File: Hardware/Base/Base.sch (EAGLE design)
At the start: 1 part

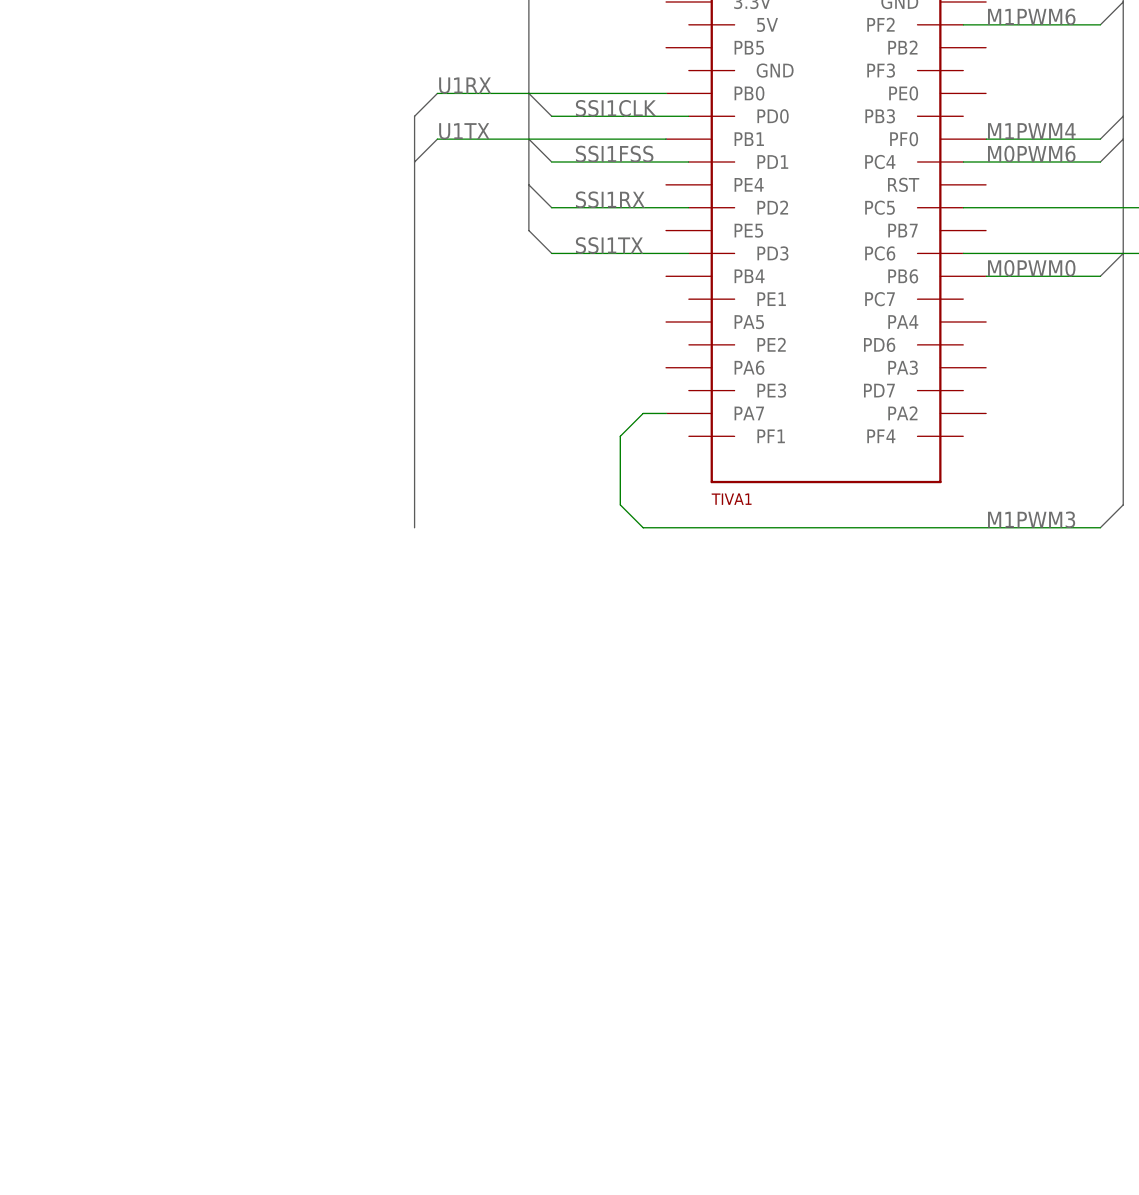
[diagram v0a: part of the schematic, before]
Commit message: Add Xbee to base schematic.
Add status LEDs to Tiva/Xbee communication.
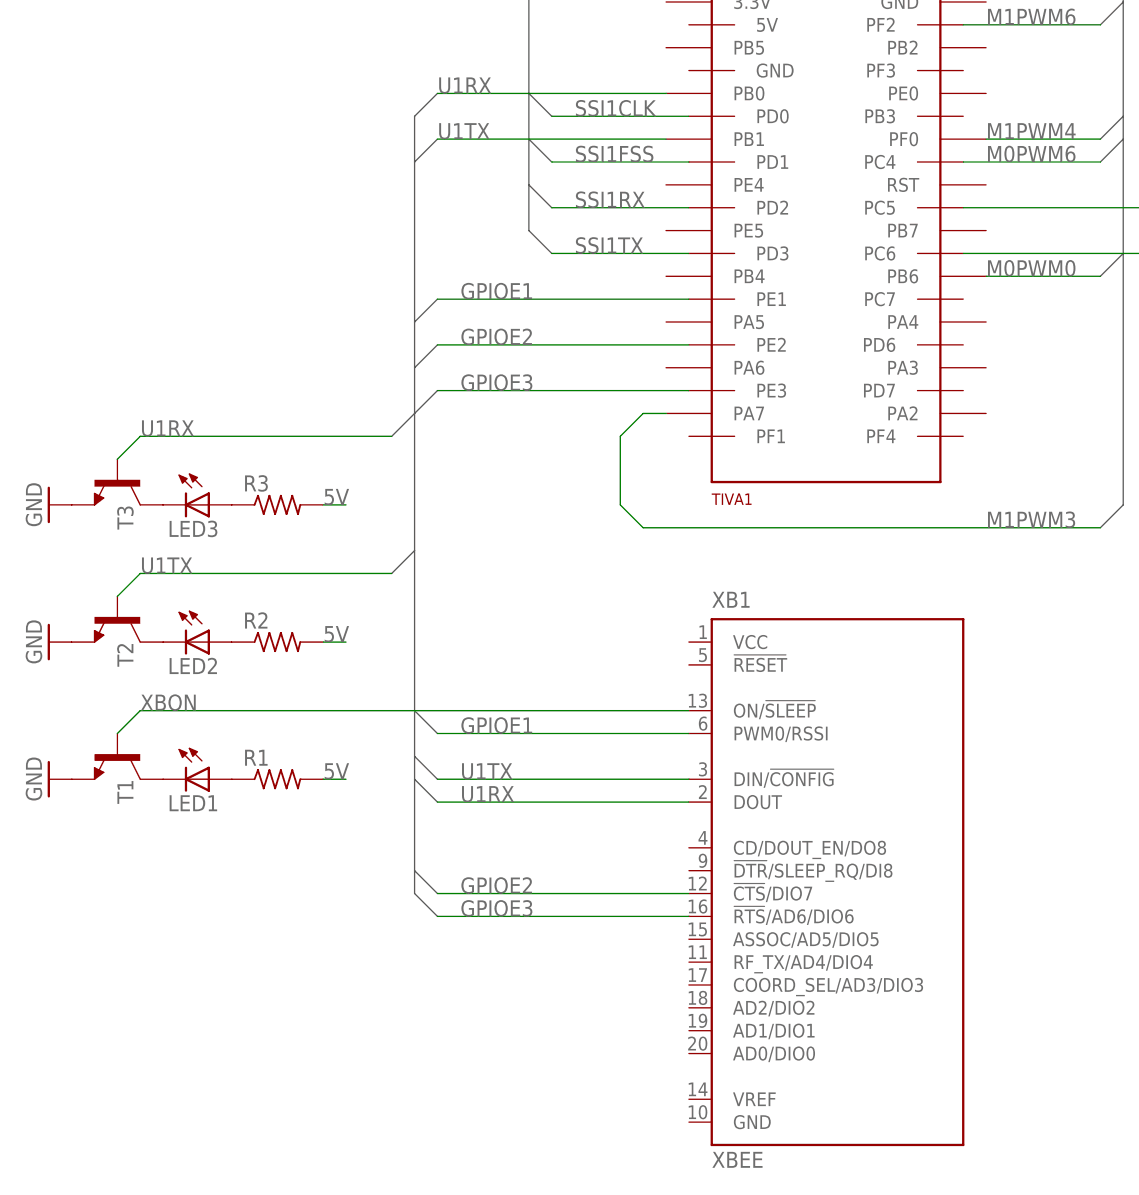
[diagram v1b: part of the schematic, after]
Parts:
- added LED1, LED2, LED3: (no value), led:LED5MM
- added R1, R2, R3: (no value), rcl:R-US_0207/7
- added T1, T2, T3: 2N3904, transistor:2N3904
- added XB1: XBEE, maxstream:XBEE
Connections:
- new net 5V: R1.2, R2.2, R3.2
- new net GND: T1.E, T2.E, T3.E
- new net GPIOE1: TIVA1.PE1, XB1.PWM0/RSSI
- new net GPIOE2: TIVA1.PE2, XB1.!CTS!/DIO7
- new net GPIOE3: TIVA1.PE3, XB1.!RTS!/AD6/DIO6
- new net N$1: LED1.C, T1.C
- new net N$2: LED2.C, T2.C
- new net N$3: LED2.A, R2.1
- new net N$4: LED1.A, R1.1
- new net N$5: LED3.C, T3.C
- new net N$6: LED3.A, R3.1
- new net XBON: T1.B, XB1.ON/!SLEEP
- net U1RX: now also T3.B, XB1.DOUT
- net U1TX: now also T2.B, XB1.DIN/!CONFIG
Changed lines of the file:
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@@
 <setting verticaltext="up"/>
 </settings>
-<grid distance="0.1" unitdist="inch" unit="mil" style="lines" multiple="1" display="yes" altdistance="0.01" altunitdist="inch" altunit="mil"/>
+<grid distance="0.1" unitdist="inch" unit="inch" style="lines" multiple="1" display="yes" altdistance="0.01" altunitdist="inch" altunit="inch"/>
 <layers>
 <layer number="1" name="Top" color="4" fill="1" visible="no" active="no"/>
@@
 <parts>
 <part name="TIVA1" library="tiva-board" deviceset="TIVA-BOARD" device=""/>
+<part name="XB1" library="maxstream" deviceset="XBEE" device=""/>
+<part name="T1" library="transistor" deviceset="2N3904" device=""/>
+<part name="R1" library="rcl" deviceset="R-US_" device="0207/7"/>
+<part name="LED1" library="led" deviceset="LED" device="5MM"/>
+<part name="GND1" library="supply1" deviceset="GND" device=""/>
+<part name="T2" library="transistor" deviceset="2N3904" device=""/>
+<part name="R2" library="rcl" deviceset="R-US_" device="0207/7"/>
+<part name="LED2" library="led" deviceset="LED" device="5MM"/>
+<part name="GND2" library="supply1" deviceset="GND" device=""/>
+<part name="T3" library="transistor" deviceset="2N3904" device=""/>
+<part name="R3" library="rcl" deviceset="R-US_" device="0207/7"/>
+<part name="LED3" library="led" deviceset="LED" device="5MM"/>
+<part name="GND3" library="supply1" deviceset="GND" device=""/>
 </parts>
 <sheets>
@@
 <instances>
 <instance part="TIVA1" gate="TIVA" x="0" y="0"/>
+<instance part="XB1" gate="G$1" x="12.7" y="-43.18"/>
+<instance part="T1" gate="G1" x="-66.04" y="-30.48" smashed="yes" rot="R270">
+<attribute name="NAME" x="-66.04" y="-33.02" size="1.778" layer="95" rot="R270"/>
+</instance>
+<instance part="R1" gate="G$1" x="-48.26" y="-33.02"/>
+<instance part="LED1" gate="G$1" x="-55.88" y="-33.02" rot="R270"/>
+<instance part="GND1" gate="1" x="-73.66" y="-33.02" rot="R270"/>
+<instance part="T2" gate="G1" x="-66.04" y="-15.24" smashed="yes" rot="R270">
+<attribute name="NAME" x="-66.04" y="-17.78" size="1.778" layer="95" rot="R270"/>
+</instance>
+<instance part="R2" gate="G$1" x="-48.26" y="-17.78"/>
+<instance part="LED2" gate="G$1" x="-55.88" y="-17.78" smashed="yes" rot="R270">
+<attribute name="NAME" x="-60.452" y="-21.336" size="1.778" layer="95"/>
+<attribute name="VALUE" x="-60.452" y="-23.495" size="1.778" layer="96"/>
+</instance>
+<instance part="GND2" gate="1" x="-73.66" y="-17.78" rot="R270"/>
+<instance part="T3" gate="G1" x="-66.04" y="0" smashed="yes" rot="R270">
+<attribute name="NAME" x="-66.04" y="-2.54" size="1.778" layer="95" rot="R270"/>
+</instance>
+<instance part="R3" gate="G$1" x="-48.26" y="-2.54"/>
+<instance part="LED3" gate="G$1" x="-55.88" y="-2.54" rot="R270"/>
+<instance part="GND3" gate="1" x="-73.66" y="-2.54" rot="R270"/>
 </instances>
 <busses>
@@
 </segment>
 </bus>
-<bus name="U1RX,U1TX">
+<bus name="U1RX,U1TX,GPIOE1,GPIOE2,GPIOE3">
 <segment>
 <wire x1="-30.48" y1="43.18" x2="-33.02" y2="40.64" width="0.762" layer="92"/>
 <wire x1="-33.02" y1="40.64" x2="-33.02" y2="35.56" width="0.762" layer="92"/>
-<wire x1="-33.02" y1="35.56" x2="-33.02" y2="-5.08" width="0.762" layer="92"/>
 <wire x1="-30.48" y1="38.1" x2="-33.02" y2="35.56" width="0.762" layer="92"/>
+<wire x1="-33.02" y1="35.56" x2="-33.02" y2="17.78" width="0.762" layer="92"/>
+<wire x1="-33.02" y1="17.78" x2="-33.02" y2="12.7" width="0.762" layer="92"/>
+<wire x1="-33.02" y1="12.7" x2="-33.02" y2="7.62" width="0.762" layer="92"/>
+<wire x1="-33.02" y1="7.62" x2="-33.02" y2="-7.62" width="0.762" layer="92"/>
+<wire x1="-33.02" y1="-7.62" x2="-33.02" y2="-25.4" width="0.762" layer="92"/>
+<wire x1="-33.02" y1="-25.4" x2="-33.02" y2="-30.48" width="0.762" layer="92"/>
+<wire x1="-33.02" y1="-30.48" x2="-33.02" y2="-33.02" width="0.762" layer="92"/>
+<wire x1="-33.02" y1="-33.02" x2="-33.02" y2="-43.18" width="0.762" layer="92"/>
+<wire x1="-33.02" y1="-43.18" x2="-33.02" y2="-45.72" width="0.762" layer="92"/>
+<wire x1="-33.02" y1="-45.72" x2="-30.48" y2="-48.26" width="0.762" layer="92"/>
+<wire x1="-33.02" y1="-43.18" x2="-30.48" y2="-45.72" width="0.762" layer="92"/>
+<wire x1="-33.02" y1="-25.4" x2="-30.48" y2="-27.94" width="0.762" layer="92"/>
+<wire x1="-33.02" y1="-30.48" x2="-30.48" y2="-33.02" width="0.762" layer="92"/>
+<wire x1="-33.02" y1="-33.02" x2="-30.48" y2="-35.56" width="0.762" layer="92"/>
+<wire x1="-33.02" y1="7.62" x2="-30.48" y2="10.16" width="0.762" layer="92"/>
+<wire x1="-33.02" y1="12.7" x2="-30.48" y2="15.24" width="0.762" layer="92"/>
+<wire x1="-33.02" y1="17.78" x2="-30.48" y2="20.32" width="0.762" layer="92"/>
+<wire x1="-33.02" y1="-7.62" x2="-35.56" y2="-10.16" width="0.762" layer="92"/>
+<wire x1="-33.02" y1="7.62" x2="-35.56" y2="5.08" width="0.762" layer="92"/>
 </segment>
 </bus>
@@
 <label x="-30.48" y="43.18" size="1.778" layer="95"/>
 </segment>
+<segment>
+<pinref part="XB1" gate="G$1" pin="DOUT"/>
+<wire x1="-30.48" y1="-35.56" x2="-2.54" y2="-35.56" width="0.1524" layer="91"/>
+<label x="-27.94" y="-35.56" size="1.778" layer="95"/>
+</segment>
+<segment>
+<pinref part="T3" gate="G1" pin="B"/>
+<wire x1="-35.56" y1="5.08" x2="-63.5" y2="5.08" width="0.1524" layer="91"/>
+<wire x1="-63.5" y1="5.08" x2="-66.04" y2="2.54" width="0.1524" layer="91"/>
+<label x="-63.5" y="5.08" size="1.778" layer="95"/>
+</segment>
 </net>
 <net name="U1TX" class="0">
@@
 <wire x1="-5.08" y1="38.1" x2="-30.48" y2="38.1" width="0.1524" layer="91"/>
 <label x="-30.48" y="38.1" size="1.778" layer="95"/>
+</segment>
+<segment>
+<pinref part="XB1" gate="G$1" pin="DIN/!CONFIG"/>
+<wire x1="-30.48" y1="-33.02" x2="-2.54" y2="-33.02" width="0.1524" layer="91"/>
+<label x="-27.94" y="-33.02" size="1.778" layer="95"/>
+</segment>
+<segment>
+<pinref part="T2" gate="G1" pin="B"/>
+<wire x1="-35.56" y1="-10.16" x2="-63.5" y2="-10.16" width="0.1524" layer="91"/>
+<wire x1="-63.5" y1="-10.16" x2="-66.04" y2="-12.7" width="0.1524" layer="91"/>
+<label x="-63.5" y="-10.16" size="1.778" layer="95"/>
 </segment>
 </net>
@@
 </segment>
 </net>
+<net name="GPIOE1" class="0">
+<segment>
+<pinref part="TIVA1" gate="TIVA" pin="PE1"/>
+<wire x1="-30.48" y1="20.32" x2="-2.54" y2="20.32" width="0.1524" layer="91"/>
+<label x="-27.94" y="20.32" size="1.778" layer="95"/>
+</segment>
+<segment>
+<pinref part="XB1" gate="G$1" pin="PWM0/RSSI"/>
+<wire x1="-30.48" y1="-27.94" x2="-2.54" y2="-27.94" width="0.1524" layer="91"/>
+<label x="-27.94" y="-27.94" size="1.778" layer="95"/>
+</segment>
+</net>
+<net name="GPIOE2" class="0">
+<segment>
+<pinref part="TIVA1" gate="TIVA" pin="PE2"/>
+<wire x1="-30.48" y1="15.24" x2="-2.54" y2="15.24" width="0.1524" layer="91"/>
+<label x="-27.94" y="15.24" size="1.778" layer="95"/>
+</segment>
+<segment>
+<pinref part="XB1" gate="G$1" pin="!CTS!/DIO7"/>
+<wire x1="-30.48" y1="-45.72" x2="-2.54" y2="-45.72" width="0.1524" layer="91"/>
+<label x="-27.94" y="-45.72" size="1.778" layer="95"/>
+</segment>
+</net>
+<net name="GPIOE3" class="0">
+<segment>
+<pinref part="TIVA1" gate="TIVA" pin="PE3"/>
+<wire x1="-30.48" y1="10.16" x2="-2.54" y2="10.16" width="0.1524" layer="91"/>
+<label x="-27.94" y="10.16" size="1.778" layer="95"/>
+</segment>
+<segment>
+<pinref part="XB1" gate="G$1" pin="!RTS!/AD6/DIO6"/>
+<wire x1="-30.48" y1="-48.26" x2="-2.54" y2="-48.26" width="0.1524" layer="91"/>
+<label x="-27.94" y="-48.26" size="1.778" layer="95"/>
+</segment>
+</net>
+<net name="XBON" class="0">
+<segment>
+<pinref part="XB1" gate="G$1" pin="ON/!SLEEP"/>
+<wire x1="-63.5" y1="-25.4" x2="-2.54" y2="-25.4" width="0.1524" layer="91"/>
+<pinref part="T1" gate="G1" pin="B"/>
+<wire x1="-66.04" y1="-27.94" x2="-63.5" y2="-25.4" width="0.1524" layer="91"/>
+<label x="-63.5" y="-25.4" size="1.778" layer="95"/>
+</segment>
+</net>
+<net name="N$1" class="0">
+<segment>
+<pinref part="T1" gate="G1" pin="C"/>
+<pinref part="LED1" gate="G$1" pin="C"/>
+</segment>
+</net>
+<net name="GND" class="0">
+<segment>
+<pinref part="T1" gate="G1" pin="E"/>
+<pinref part="GND1" gate="1" pin="GND"/>
+</segment>
+<segment>
+<pinref part="T2" gate="G1" pin="E"/>
+<pinref part="GND2" gate="1" pin="GND"/>
+</segment>
+<segment>
+<pinref part="T3" gate="G1" pin="E"/>
+<pinref part="GND3" gate="1" pin="GND"/>
+</segment>
+</net>
+<net name="N$4" class="0">
+<segment>
+<pinref part="LED1" gate="G$1" pin="A"/>
+<pinref part="R1" gate="G$1" pin="1"/>
+</segment>
+</net>
+<net name="N$2" class="0">
+<segment>
+<pinref part="T2" gate="G1" pin="C"/>
+<pinref part="LED2" gate="G$1" pin="C"/>
+</segment>
+</net>
+<net name="N$3" class="0">
+<segment>
+<pinref part="LED2" gate="G$1" pin="A"/>
+<pinref part="R2" gate="G$1" pin="1"/>
+</segment>
+</net>
+<net name="N$5" class="0">
+<segment>
+<pinref part="T3" gate="G1" pin="C"/>
+<pinref part="LED3" gate="G$1" pin="C"/>
+</segment>
+</net>
+<net name="N$6" class="0">
+<segment>
+<pinref part="LED3" gate="G$1" pin="A"/>
+<pinref part="R3" gate="G$1" pin="1"/>
+</segment>
+</net>
+<net name="5V" class="0">
+<segment>
+<pinref part="R3" gate="G$1" pin="2"/>
+<wire x1="-43.18" y1="-2.54" x2="-40.64" y2="-2.54" width="0.1524" layer="91"/>
+<label x="-43.18" y="-2.54" size="1.778" layer="95"/>
+</segment>
+<segment>
+<pinref part="R2" gate="G$1" pin="2"/>
+<wire x1="-43.18" y1="-17.78" x2="-40.64" y2="-17.78" width="0.1524" layer="91"/>
+<label x="-43.18" y="-17.78" size="1.778" layer="95"/>
+</segment>
+<segment>
+<pinref part="R1" gate="G$1" pin="2"/>
+<wire x1="-43.18" y1="-33.02" x2="-40.64" y2="-33.02" width="0.1524" layer="91"/>
+<label x="-43.18" y="-33.02" size="1.778" layer="95"/>
+</segment>
+</net>

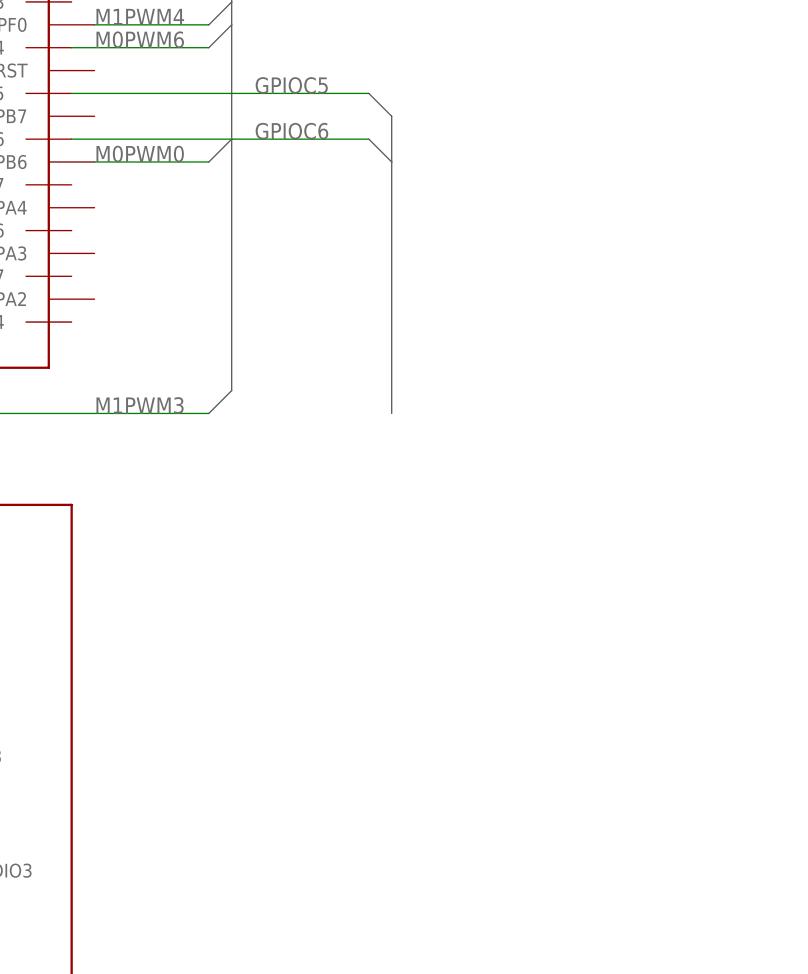
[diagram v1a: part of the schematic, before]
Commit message: Add rotary encoder to base schematic.
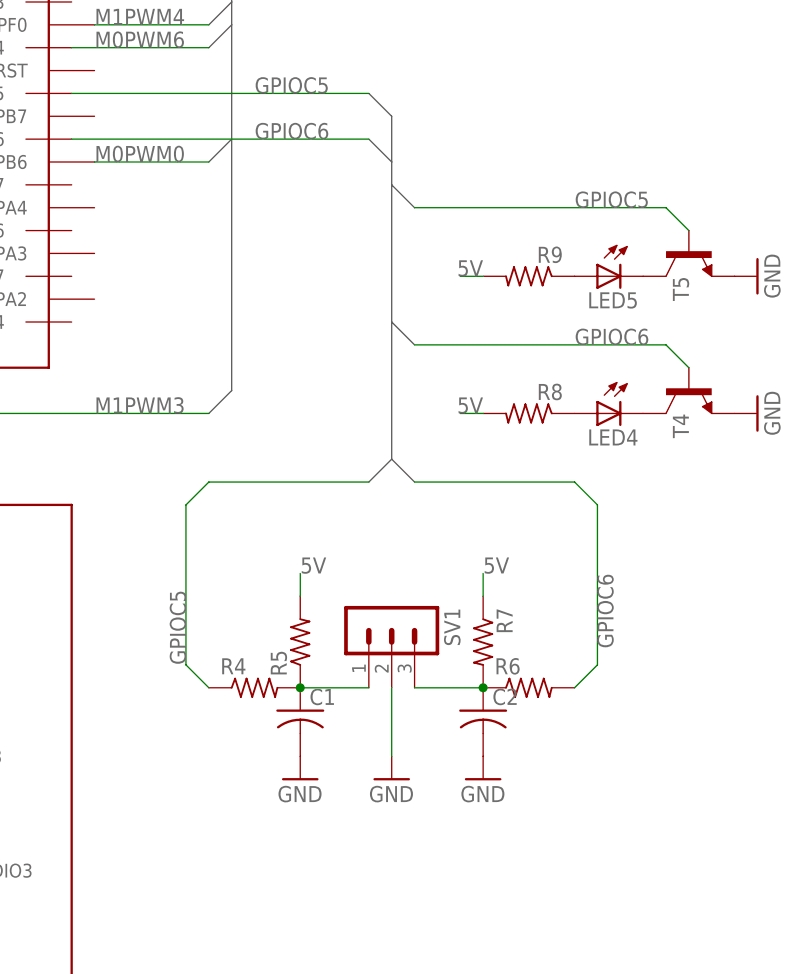
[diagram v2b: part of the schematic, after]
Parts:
- added C1, C2: (no value), rcl:C-US025-025X050
- added LED4, LED5: (no value), led:LED5MM
- added R4, R5, R6, R7, R8, R9: (no value), rcl:R-US_0207/7
- added SV1: (no value), con-lstb:MA03-1
- added T4, T5: 2N3904, transistor:2N3904
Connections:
- new net N$10: LED4.A, R8.1
- new net N$11: LED5.C, T5.C
- new net N$12: LED5.A, R9.1
- new net N$7: C1.1, R4.2, R5.1, SV1.1
- new net N$8: C2.1, R6.1, R7.2, SV1.3
- new net N$9: LED4.C, T4.C
- net 5V: now also R5.2, R7.1, R8.2, R9.2
- net GND: now also C1.2, C2.2, SV1.2, T4.E, T5.E
- net GPIOC5: now also R4.1, T5.B
- net GPIOC6: now also R6.2, T4.B
